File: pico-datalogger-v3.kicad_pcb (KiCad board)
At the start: 2 copper layers, 130 x 65 mm, 60 parts, among them IC1 LM66200DRLR, J1 JST-PH2 Bat, J11 Conn_I2C1, J12 Conn_UART_5V, J13 THT_I2C1, J14 THT_I2C0, J17 Disp_THT, J2 Conn_Pico_Left, J3 Conn_Pico_Right, J4 SM06B-GHS-TB_LF_SN, J6 Conn_Display, J9 Conn_I2C0, Q1 AO3401A, Q2 AO3401A, SW1 SW_Push, SW2 SW_Push, SW3 SW_Push, SW4 SW_Push, SW5 SW_Push, U1 74LVC2G74, U2 PCF8523T, U4 XTSD, U5 SCD40_Breakout, U6 AHT20, U7 RFM95W-868S2, Y1 Crystal

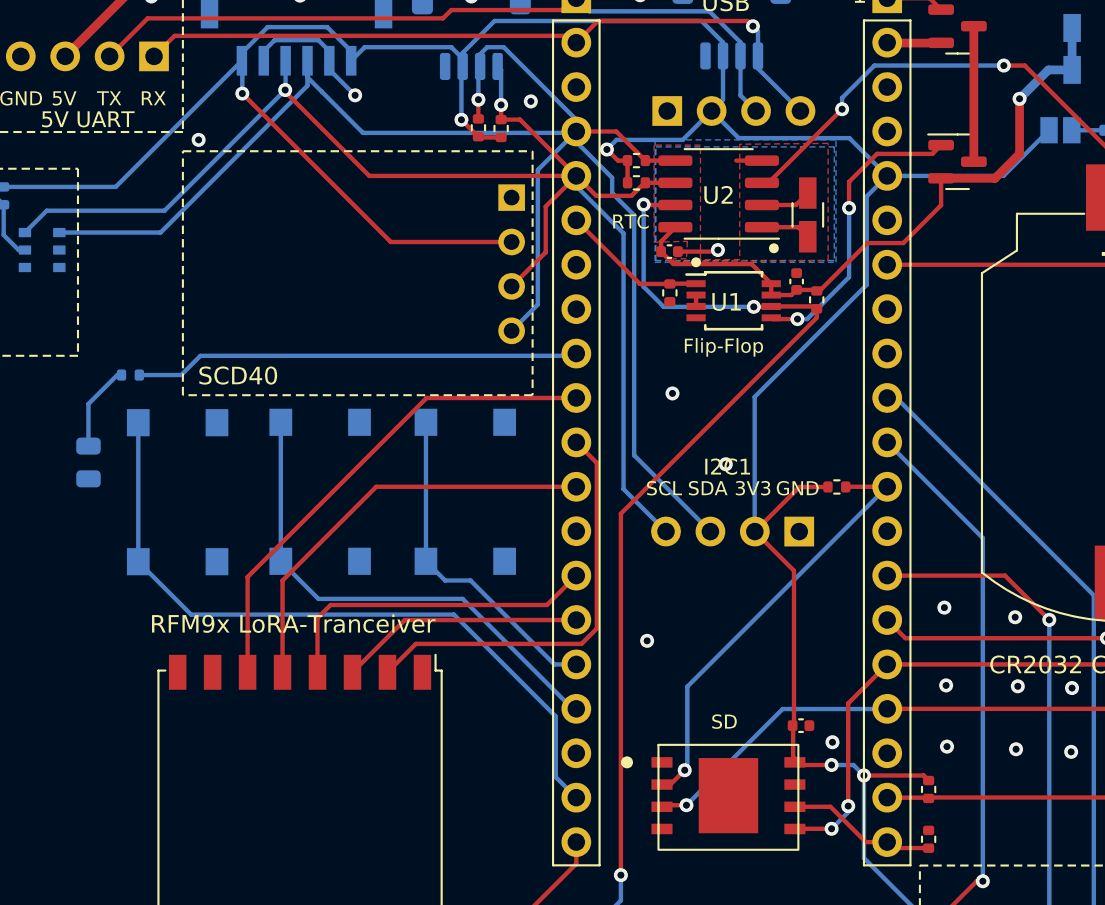
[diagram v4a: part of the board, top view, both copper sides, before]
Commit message: swapped additional pins to simplify routing
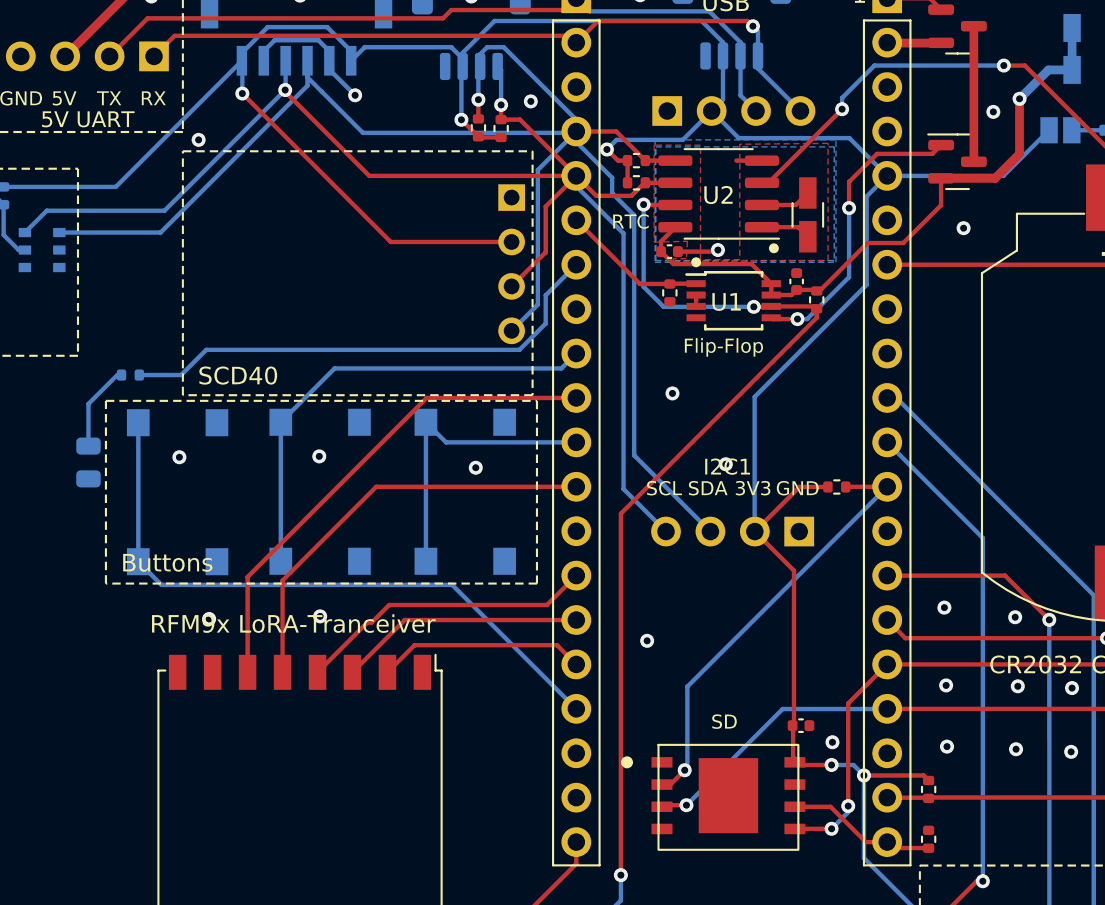
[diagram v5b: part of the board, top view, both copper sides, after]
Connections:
- J2 pad 11: MISO1 -> SWA
- J2 pad 16: SWA -> MISO1
- J2 pad 17: SWB -> SWC
- J2 pad 19: SWC -> unconnected-(J2-Pin_19-Pad19)
- J2 pad 7: unconnected-(J2-Pin_7-Pad7) -> SWD
- J2 pad 9: SWD -> SWB
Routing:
- net MISO1: track 24.1 -> 11.9 mm
- net SWC: track 40.6 -> 36.5 mm
- net SWD: track 25.5 -> 28.6 mm
- net SWA: track 19.0 -> 17.0 mm
- net SWB: track 28.3 -> 26.5 mm
- net SCLK1: track 18.9 -> 17.1 mm
- net GND: vias 29 -> 36
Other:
- board text added: "Buttons"

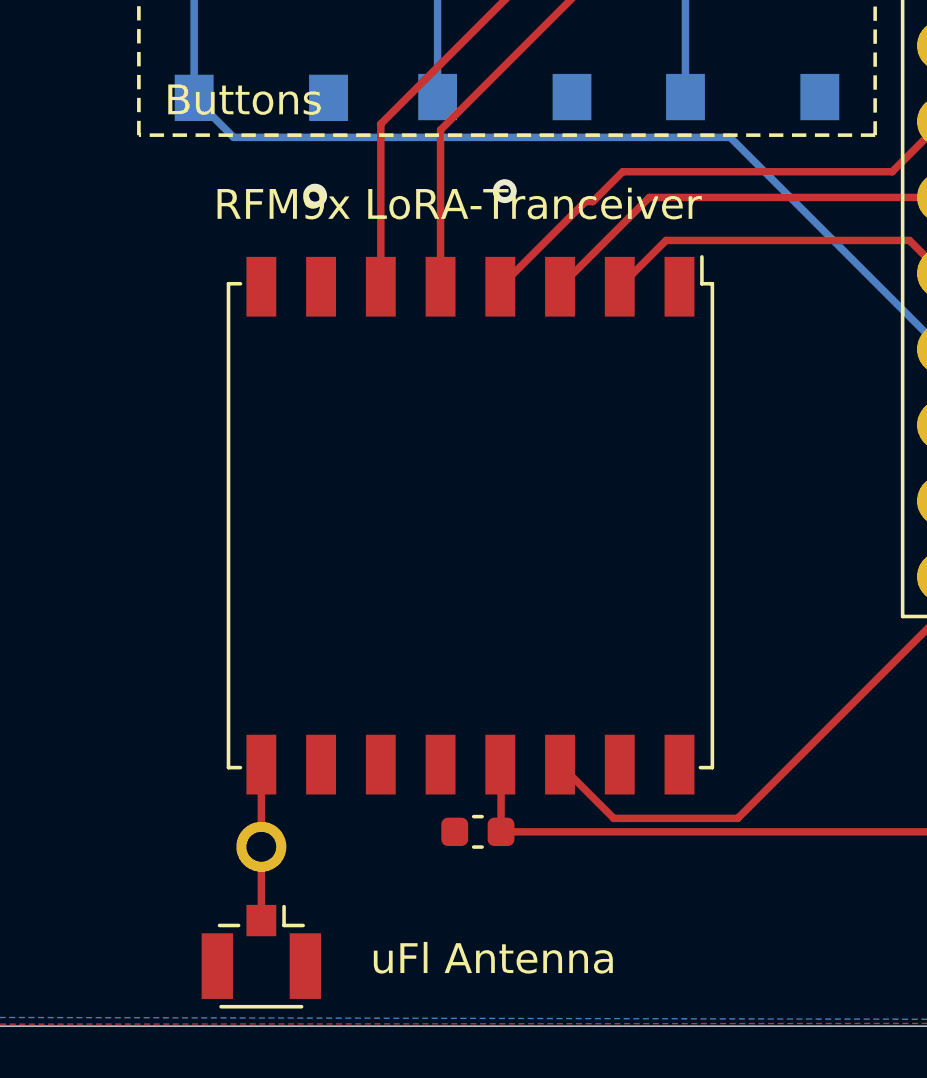
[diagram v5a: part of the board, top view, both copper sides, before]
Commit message: added GND-vias for LoRa
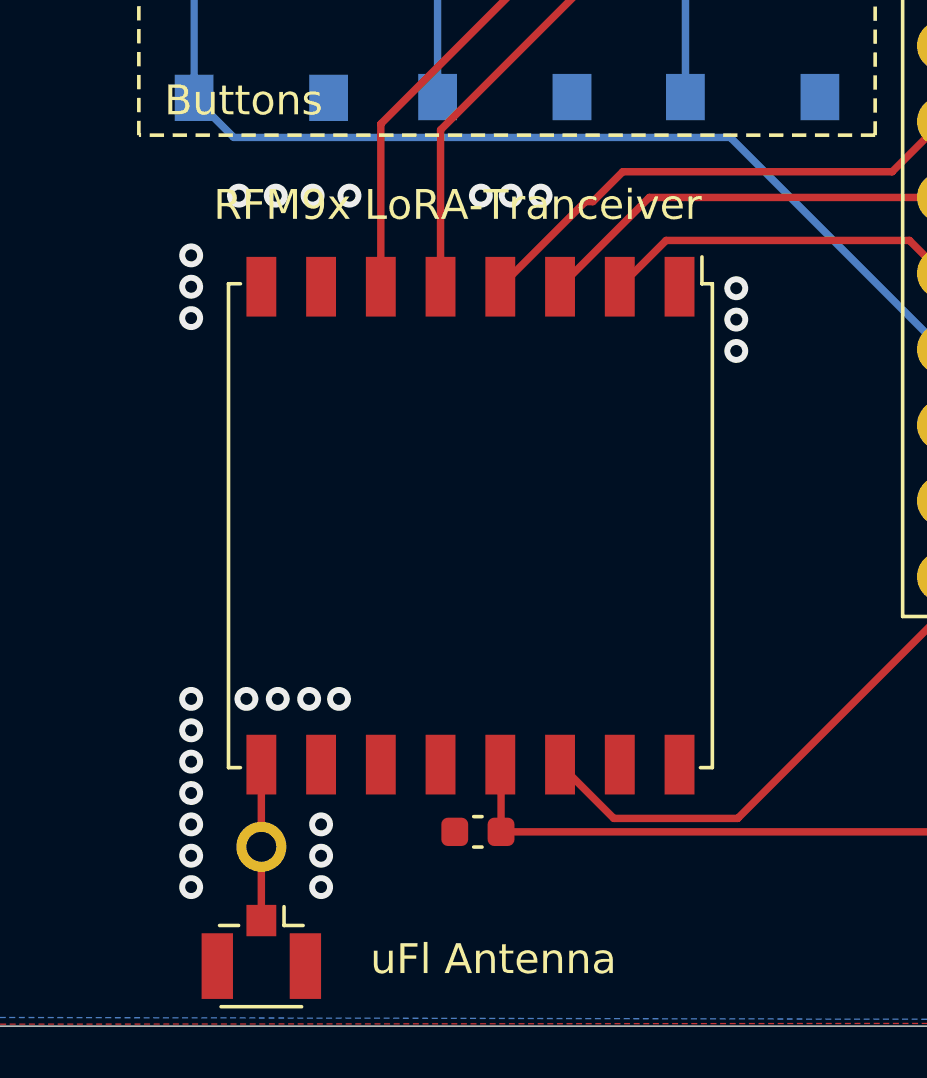
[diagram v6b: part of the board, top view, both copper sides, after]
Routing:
- net GND: vias 36 -> 61
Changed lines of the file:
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@@
   (segment (start 147.66 116.14) (end 147.75 116.05) (width 0.25) (layer "F.Cu") (net 2))
   (via (at 124.95 127.85) (size 0.8) (drill 0.4) (layers "F.Cu" "B.Cu") (free) (net 2))
+  (via (at 114.5 154) (size 0.8) (drill 0.4) (layers "F.Cu" "B.Cu") (free) (net 2))
   (via (at 164.9 141) (size 0.8) (drill 0.4) (layers "F.Cu" "B.Cu") (free) (net 2))
   (via (at 164.75 137.05) (size 0.8) (drill 0.4) (layers "F.Cu" "B.Cu") (free) (net 2))
@@
   (via (at 173.05 145.25) (size 0.8) (drill 0.4) (layers "F.Cu" "B.Cu") (free) (net 2))
   (via (at 177.75 107.1) (size 0.8) (drill 0.4) (layers "F.Cu" "B.Cu") (net 2))
+  (via (at 114.5 160.3) (size 0.8) (drill 0.4) (layers "F.Cu" "B.Cu") (free) (net 2))
   (via (at 160.8 140.95) (size 0.8) (drill 0.4) (layers "F.Cu" "B.Cu") (free) (net 2))
+  (via (at 126.2 137.15) (size 0.8) (drill 0.4) (layers "F.Cu" "B.Cu") (free) (net 2))
   (via (at 145.15 124.25) (size 0.8) (drill 0.4) (layers "F.Cu" "B.Cu") (free) (net 2))
   (via (at 167.95 144.75) (size 0.8) (drill 0.4) (layers "F.Cu" "B.Cu") (free) (net 2))
   (via (at 160.85 144.45) (size 0.8) (drill 0.4) (layers "F.Cu" "B.Cu") (free) (net 2))
+  (via (at 118.85 158.2) (size 0.8) (drill 0.4) (layers "F.Cu" "B.Cu") (free) (net 2))
   (via (at 163.5 108.15) (size 0.8) (drill 0.4) (layers "F.Cu" "B.Cu") (free) (net 2))
   (via (at 148.2 128.3) (size 0.8) (drill 0.4) (layers "F.Cu" "B.Cu") (free) (net 2))
+  (via (at 132.75 142.35) (size 0.8) (drill 0.4) (layers "F.Cu" "B.Cu") (free) (net 2))
   (via (at 137.05 107.55) (size 0.8) (drill 0.4) (layers "F.Cu" "B.Cu") (free) (net 2))
   (via (at 143.7 138.4) (size 0.8) (drill 0.4) (layers "F.Cu" "B.Cu") (free) (net 2))
   (via (at 123.85 101.5) (size 0.8) (drill 0.4) (layers "F.Cu" "B.Cu") (free) (net 2))
+  (via (at 114.5 141.25) (size 0.8) (drill 0.4) (layers "F.Cu" "B.Cu") (free) (net 2))
   (via (at 133.9 128.5) (size 0.8) (drill 0.4) (layers "F.Cu" "B.Cu") (free) (net 2))
   (via (at 127 107.2) (size 0.8) (drill 0.4) (layers "F.Cu" "B.Cu") (net 2))
+  (via (at 119.8 137.15) (size 0.8) (drill 0.4) (layers "F.Cu" "B.Cu") (free) (net 2))
+  (via (at 114.5 156.1) (size 0.8) (drill 0.4) (layers "F.Cu" "B.Cu") (free) (net 2))
   (via (at 180.95 104.5) (size 0.8) (drill 0.4) (layers "F.Cu" "B.Cu") (net 2))
   (via (at 143.3 101.48) (size 0.8) (drill 0.4) (layers "F.Cu" "B.Cu") (free) (net 2))
   (via (at 176.95 159.4) (size 0.8) (drill 0.4) (layers "F.Cu" "B.Cu") (free) (net 2))
+  (via (at 114.5 158.2) (size 0.8) (drill 0.4) (layers "F.Cu" "B.Cu") (free) (net 2))
   (via (at 178.15 152.75) (size 0.8) (drill 0.4) (layers "F.Cu" "B.Cu") (free) (net 2))
+  (via (at 119.45 154) (size 0.8) (drill 0.4) (layers "F.Cu" "B.Cu") (free) (net 2))
   (via (at 160.7 136.5) (size 0.8) (drill 0.4) (layers "F.Cu" "B.Cu") (free) (net 2))
-  (via (at 118.65 137.15) (size 0.8) (drill 0.4) (layers "F.Cu" "B.Cu") (free) (net 2))
+  (via (at 132.75 141.3) (size 0.8) (drill 0.4) (layers "F.Cu" "B.Cu") (free) (net 2))
+  (via (at 118.566666 137.15) (size 0.8) (drill 0.4) (layers "F.Cu" "B.Cu") (free) (net 2))
+  (via (at 118.85 160.3) (size 0.8) (drill 0.4) (layers "F.Cu" "B.Cu") (free) (net 2))
+  (via (at 125.2 137.15) (size 0.8) (drill 0.4) (layers "F.Cu" "B.Cu") (free) (net 2))
   (via (at 180.9 106.05) (size 0.8) (drill 0.4) (layers "F.Cu" "B.Cu") (net 2))
+  (via (at 114.5 159.25) (size 0.8) (drill 0.4) (layers "F.Cu" "B.Cu") (free) (net 2))
   (via (at 133.65 101.55) (size 0.8) (drill 0.4) (layers "F.Cu" "B.Cu") (free) (net 2))
   (via (at 118.05 109.75) (size 0.8) (drill 0.4) (layers "F.Cu" "B.Cu") (free) (net 2))
+  (via (at 118.45 154) (size 0.8) (drill 0.4) (layers "F.Cu" "B.Cu") (free) (net 2))
+  (via (at 118.85 159.25) (size 0.8) (drill 0.4) (layers "F.Cu" "B.Cu") (free) (net 2))
   (via (at 168 141.1) (size 0.8) (drill 0.4) (layers "F.Cu" "B.Cu") (free) (net 2))
+  (via (at 114.5 157.15) (size 0.8) (drill 0.4) (layers "F.Cu" "B.Cu") (free) (net 2))
+  (via (at 114.5 139.15) (size 0.8) (drill 0.4) (layers "F.Cu" "B.Cu") (free) (net 2))
   (via (at 116.95 127.9) (size 0.8) (drill 0.4) (layers "F.Cu" "B.Cu") (free) (net 2))
   (via (at 170.45 144.7) (size 0.8) (drill 0.4) (layers "F.Cu" "B.Cu") (free) (net 2))
+  (via (at 116.1 137.15) (size 0.8) (drill 0.4) (layers "F.Cu" "B.Cu") (free) (net 2))
+  (via (at 116.35 154) (size 0.8) (drill 0.4) (layers "F.Cu" "B.Cu") (free) (net 2))
+  (via (at 117.333333 137.15) (size 0.8) (drill 0.4) (layers "F.Cu" "B.Cu") (free) (net 2))
   (via (at 161.8 114.8) (size 0.8) (drill 0.4) (layers "F.Cu" "B.Cu") (free) (net 2))
   (via (at 154.3 144.2) (size 0.8) (drill 0.4) (layers "F.Cu" "B.Cu") (free) (net 2))
+  (via (at 117.4 154) (size 0.8) (drill 0.4) (layers "F.Cu" "B.Cu") (free) (net 2))
   (via (at 175.4 152.8) (size 0.8) (drill 0.4) (layers "F.Cu" "B.Cu") (free) (net 2))
-  (via (at 125 137) (size 0.8) (drill 0.4) (layers "F.Cu" "B.Cu") (free) (net 2))
+  (via (at 124.2 137.15) (size 0.8) (drill 0.4) (layers "F.Cu" "B.Cu") (free) (net 2))
   (via (at 115.35 101.55) (size 0.8) (drill 0.4) (layers "F.Cu" "B.Cu") (free) (net 2))
   (via (at 147.75 116.05) (size 0.8) (drill 0.4) (layers "F.Cu" "B.Cu") (free) (net 2))
+  (via (at 132.75 140.25) (size 0.8) (drill 0.4) (layers "F.Cu" "B.Cu") (free) (net 2))
   (via (at 168.2 160.05) (size 0.8) (drill 0.4) (layers "F.Cu" "B.Cu") (net 2))
+  (via (at 114.5 155.05) (size 0.8) (drill 0.4) (layers "F.Cu" "B.Cu") (free) (net 2))
+  (via (at 114.5 140.2) (size 0.8) (drill 0.4) (layers "F.Cu" "B.Cu") (free) (net 2))
   (segment (start 125.525 105.225) (end 125.525 105.725) (width 0.25) (layer "B.Cu") (net 2))
   (segment (start 168.2 160.05) (end 168.5 160.35) (width 0.25) (layer "B.Cu") (net 2))

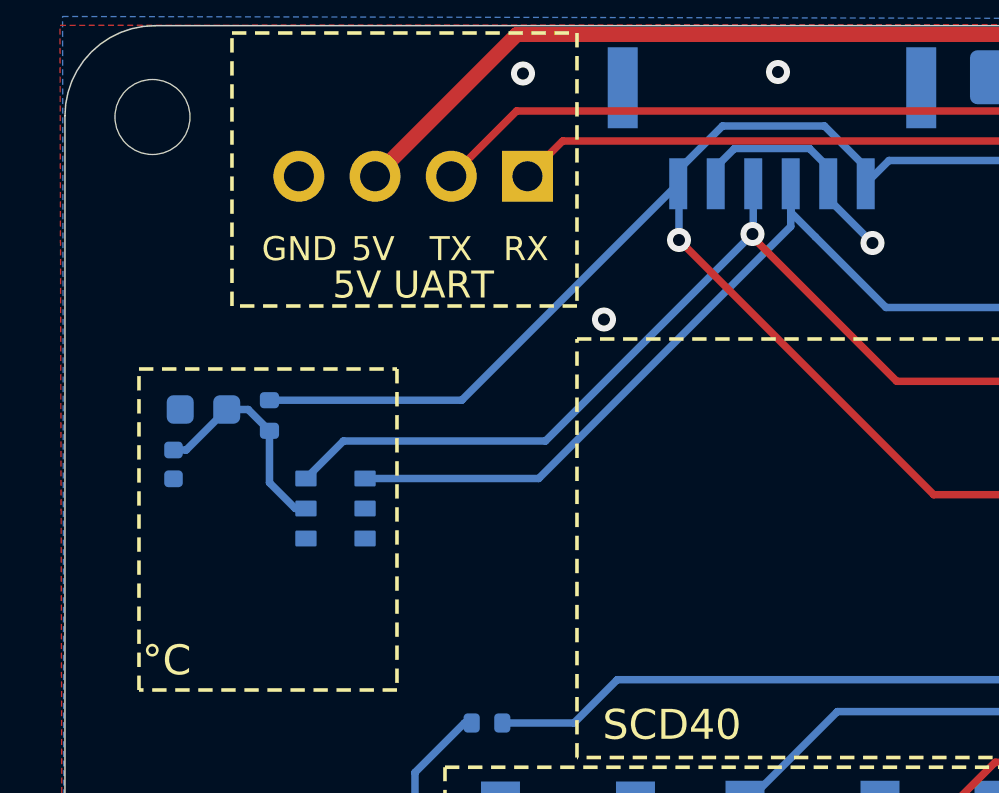
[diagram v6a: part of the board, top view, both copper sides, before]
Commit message: fine tune AHT20 layout and add cutout
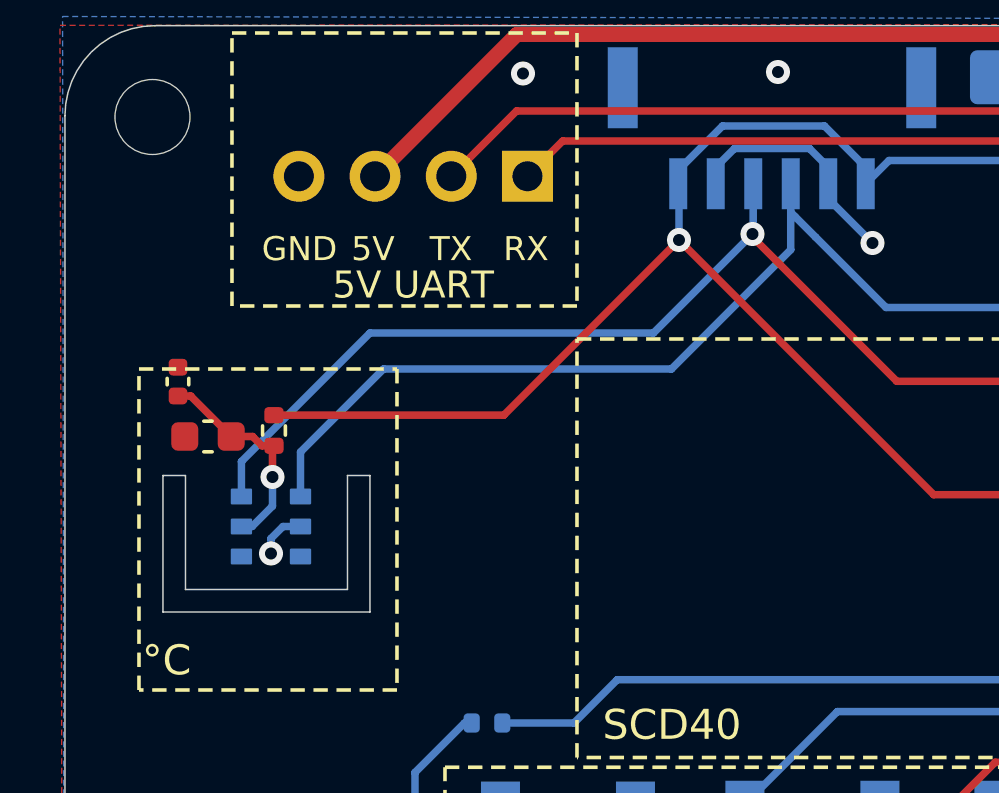
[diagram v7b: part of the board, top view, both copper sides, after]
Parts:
- C4, C5, R8: moved to F.Cu
- moved C4 2.76 mm to (103.8, 111.8), turned to 90 degrees
- moved U6 2.23 mm to (107.0, 116.7)
- moved C5 0.91 mm to (104.8, 113.7)
- moved R8 0.52 mm to (107.0, 113.5)
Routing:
- net SCL: track 84.2 -> 87.3 mm
- net SDA: track 93.9 -> 96.7 mm
- net GND: track 18.1 -> 19.8 mm
- net +3V3: track 225.4 -> 224.7 mm
- net Net-(U6-VDD): track 7.35 -> 7.23 mm, vias 0 -> 1
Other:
- outline, holes or cut-outs redrawn

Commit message: fixes for production files
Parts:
- BT2: footprint Battery:BatteryHolder_Keystone_2462_2xAA -> user:BatteryHolder_Keystone_2462_2xAA
- moved BT2 0.05 mm to (206.8, 105.2)
